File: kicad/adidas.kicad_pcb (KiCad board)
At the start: 2 copper layers, 2 parts

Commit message: v0.1
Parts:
- removed the G*** at (152.4, 96.5)
- added G***: LOGO, DEAD10C5:Adidas, F.Cu at (147.3, 94.0)
- moved G*** 69.7 mm to (221.0, 91.4)

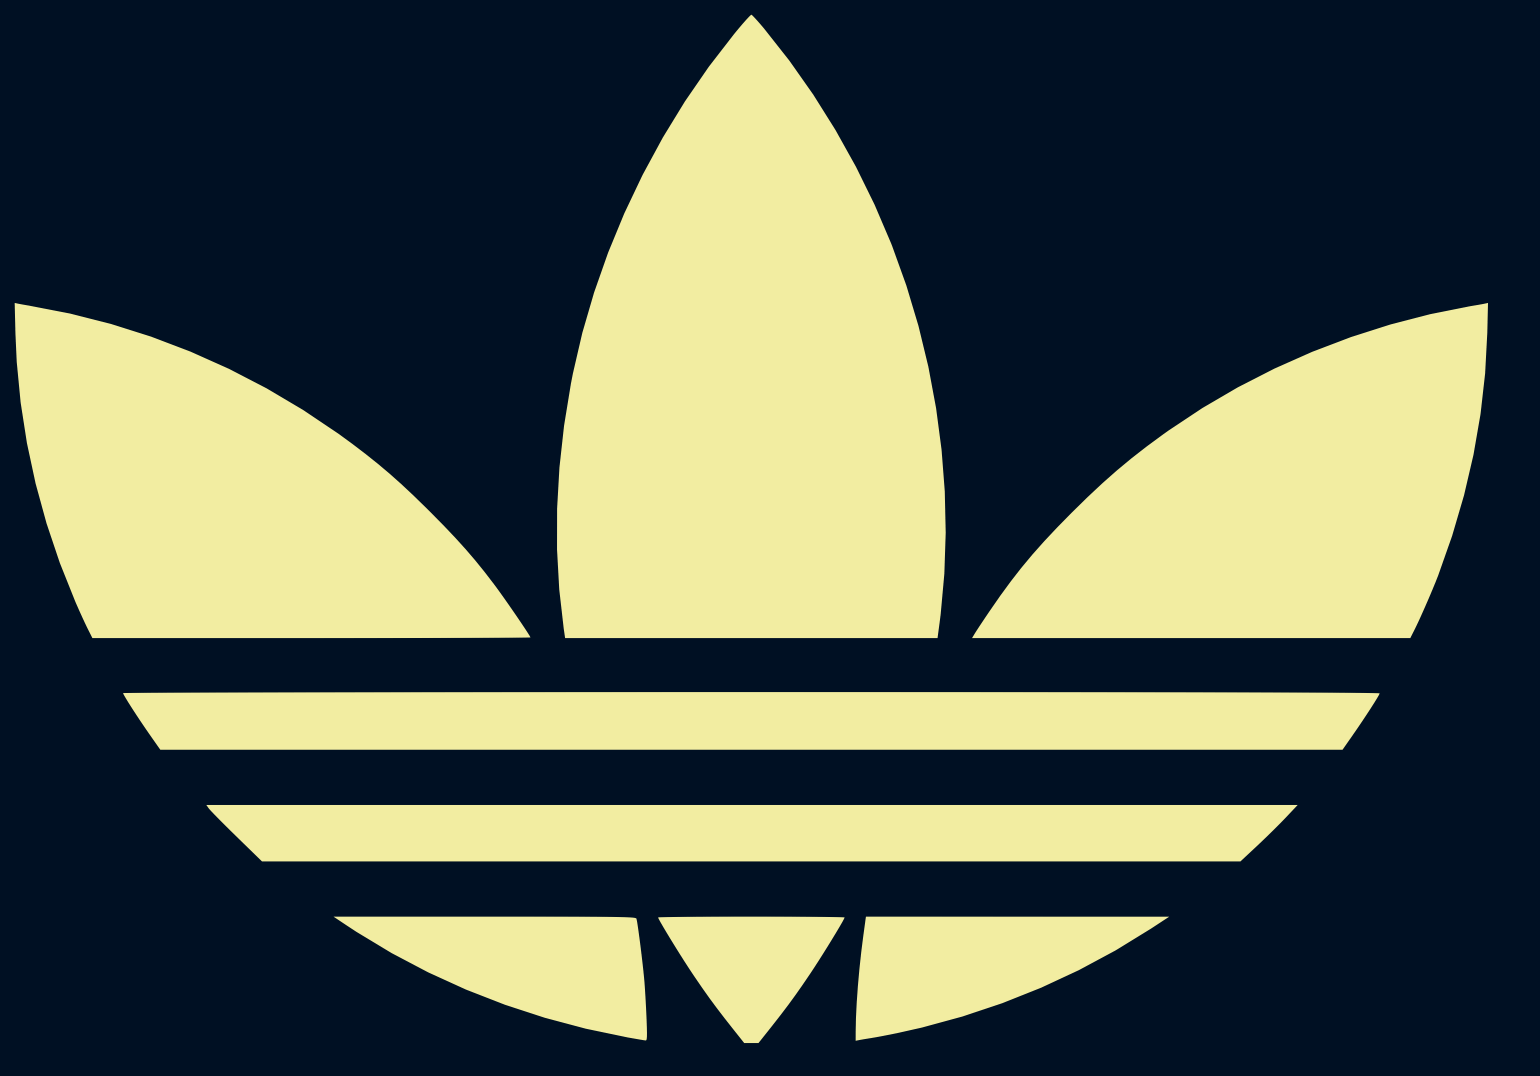
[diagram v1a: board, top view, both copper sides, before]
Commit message: resized art and created outline
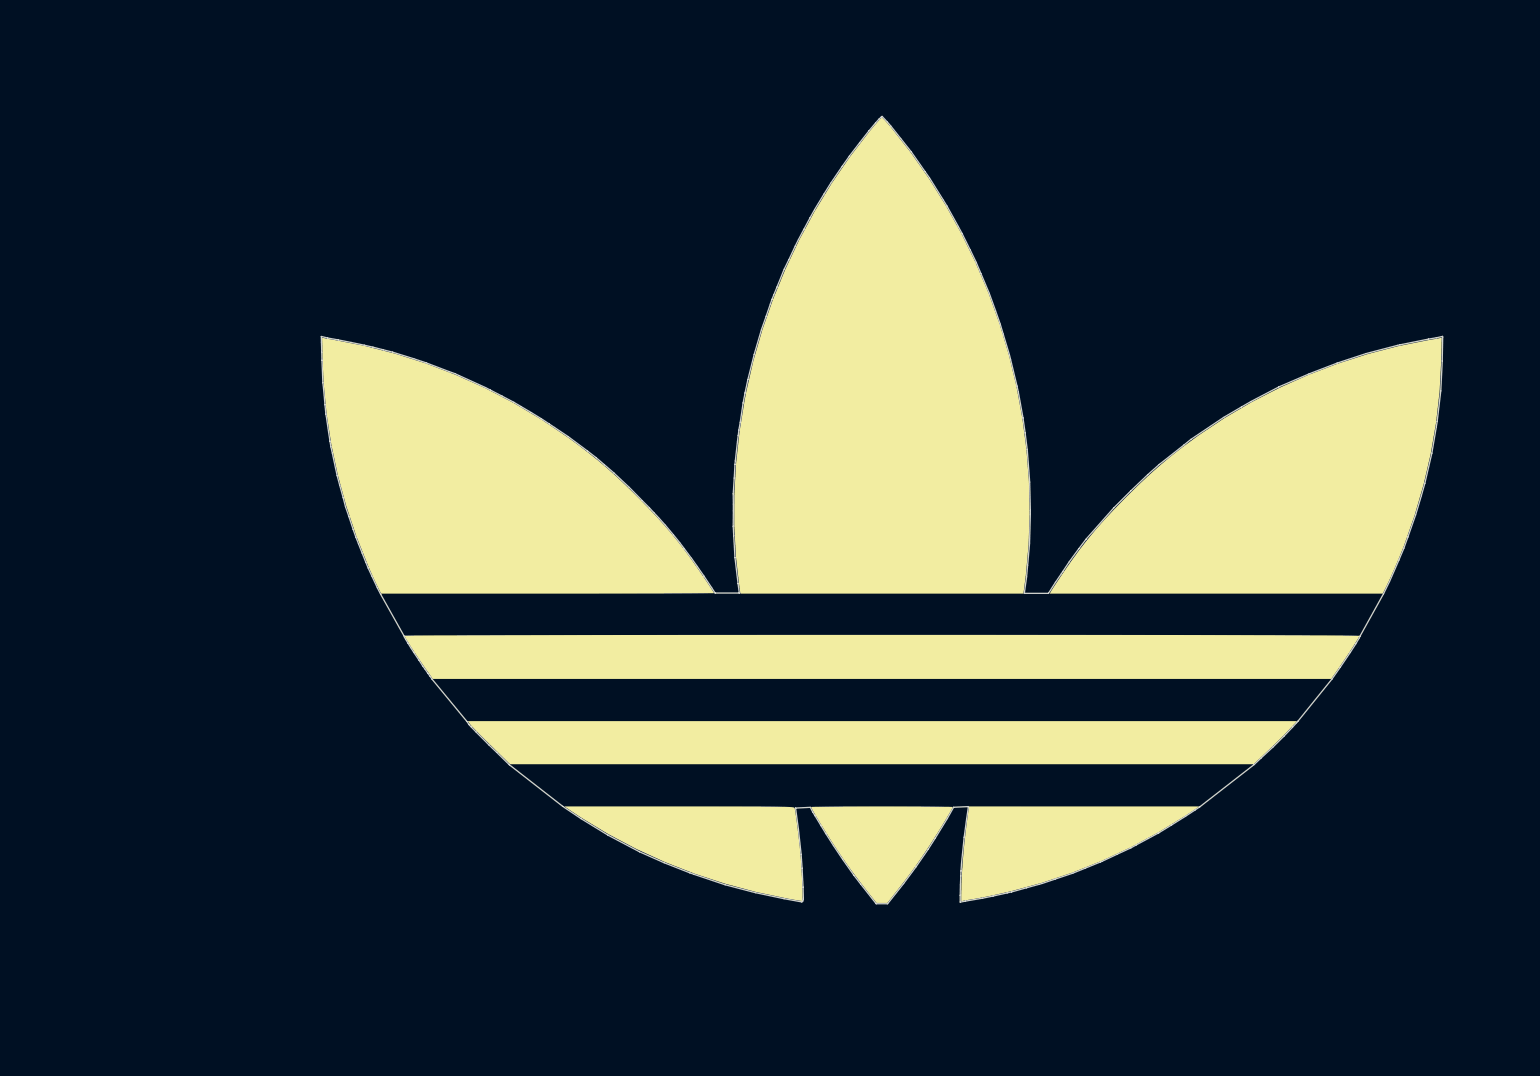
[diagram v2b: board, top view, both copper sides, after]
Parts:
- removed the G*** at (147.3, 94.0)
- added G***: LOGO, Adidas:Adidas_Logo, F.Cu at (165.1, 91.4)
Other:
- board outline added: 152.7 x 107.2 mm

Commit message: updates
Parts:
- added REF**: MountingHole_4.5mm, MountingHole:MountingHole_4.5mm, F.Cu at (165.0, 49.4)
- added REF**: BatteryHolder_Keystone_3002_1x2032, Battery:BatteryHolder_Keystone_3002_1x2032, B.Cu at (164.8, 120.4)
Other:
- board text added: "0.2000 mm / 0.0000 mm"
- board text added: "0.3000 mm"
- board text added: "1.6000 mm"
- board text added: "152.7000 mm x 107.2200 mm"
- board text added: "2"
- board text added: "BOARD CHARACTERISTICS"
- board text added: "Board Thickness:"
- board text added: "Board overall dimensions:"
- board text added: "Castellated pads:"
- board text added: "Copper Finish:"
- board text added: "Copper Layer Count:"
- board text added: "Edge card connectors:"
- board text added: "Impedance Control:"
- board text added: "Min hole diameter:"
- board text added: "Min track/spacing:"
- board text added: "No"
- board text added: "None"
- board text added: "Plated Board Edge:"

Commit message: add mpu6050 part
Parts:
- removed the G*** at (221.0, 91.4)
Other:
- board text added: "мне нравится двигать его двигать его"

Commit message: add 6050 footprint
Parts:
- added REF**: QFN50P400X400X95-24N, Library:QFN50P400X400X95-24N, B.Cu at (165.6, 99.6)
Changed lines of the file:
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@@
     )
+  )
+  (footprint "Library:QFN50P400X400X95-24N" (layer "B.Cu")
+    (at 165.6 99.6 180)
+    (attr through_hole)
+    (fp_text reference "REF**" (at 1.17756 3.64297) (layer "B.SilkS") hide
+      (effects (font (size 1.002189 1.002189) (thickness 0.15)) (justify mirror))
+    )
+    (fp_text value "QFN50P400X400X95-24N" (at 10.71558 -3.369915) (layer "B.Fab") hide
+      (effects (font (size 1.001457 1.001457) (thickness 0.15)) (justify mirror))
+    )
+    (fp_line (start 2.05 -1.56) (end 2.05 -2.05) (layer "B.SilkS") (width 0.127))
+    (fp_line (start -2.05 -2.05) (end -2.05 -1.56) (layer "B.SilkS") (width 0.127))
+    (fp_line (start 2.05 -2.05) (end 1.56 -2.05) (layer "B.SilkS") (width 0.127))
+    (fp_line (start -1.56 -2.05) (end -2.05 -2.05) (layer "B.SilkS") (width 0.127))
+    (fp_line (start 2.05 2.05) (end 2.05 1.56) (layer "B.SilkS") (width 0.127))
+    (fp_line (start -1.56 2.05) (end -2.05 2.05) (layer "B.SilkS") (width 0.127))
+    (fp_line (start 1.56 2.05) (end 2.05 2.05) (layer "B.SilkS") (width 0.127))
+    (fp_line (start -2.05 1.56) (end -2.05 2.05) (layer "B.SilkS") (width 0.127))
+    (fp_circle (center -3 1.3) (end -2.9 1.3) (layer "B.SilkS") (width 0.2) (fill none))
+    (fp_line (start -2.62 -2.62) (end -2.62 2.62) (layer "B.CrtYd") (width 0.05))
+    (fp_line (start 2.62 2.62) (end 2.62 -2.62) (layer "B.CrtYd") (width 0.05))
+    (fp_line (start -2.62 2.62) (end 2.62 2.62) (layer "B.CrtYd") (width 0.05))
+    (fp_line (start 2.62 -2.62) (end -2.62 -2.62) (layer "B.CrtYd") (width 0.05))
+    (fp_line (start -2.05 2.05) (end -2.05 -2.05) (layer "B.Fab") (width 0.127))
+    (fp_line (start 2.05 2.05) (end 2.05 -2.05) (layer "B.Fab") (width 0.127))
+    (fp_line (start 2.05 2.05) (end -2.05 2.05) (layer "B.Fab") (width 0.127))
+    (fp_line (start 2.05 -2.05) (end -2.05 -2.05) (layer "B.Fab") (width 0.127))
+    (pad "1" smd rect (at -1.97 1.25 180) (size 0.79 0.26) (layers "B.Cu" "B.Paste" "B.Mask"))
+    (pad "2" smd rect (at -1.97 0.75 180) (size 0.79 0.26) (layers "B.Cu" "B.Paste" "B.Mask"))
+    (pad "3" smd rect (at -1.97 0.25 180) (size 0.79 0.26) (layers "B.Cu" "B.Paste" "B.Mask"))
+    (pad "4" smd rect (at -1.97 -0.25 180) (size 0.79 0.26) (layers "B.Cu" "B.Paste" "B.Mask"))
+    (pad "5" smd rect (at -1.97 -0.75 180) (size 0.79 0.26) (layers "B.Cu" "B.Paste" "B.Mask"))
+    (pad "6" smd rect (at -1.97 -1.25 180) (size 0.79 0.26) (layers "B.Cu" "B.Paste" "B.Mask"))
+    (pad "7" smd rect (at -1.25 -1.97 90) (size 0.79 0.26) (layers "B.Cu" "B.Paste" "B.Mask"))
+    (pad "8" smd rect (at -0.75 -1.97 90) (size 0.79 0.26) (layers "B.Cu" "B.Paste" "B.Mask"))
+    (pad "9" smd rect (at -0.25 -1.97 90) (size 0.79 0.26) (layers "B.Cu" "B.Paste" "B.Mask"))
+    (pad "10" smd rect (at 0.25 -1.97 90) (size 0.79 0.26) (layers "B.Cu" "B.Paste" "B.Mask"))
+    (pad "11" smd rect (at 0.75 -1.97 90) (size 0.79 0.26) (layers "B.Cu" "B.Paste" "B.Mask"))
+    (pad "12" smd rect (at 1.25 -1.97 90) (size 0.79 0.26) (layers "B.Cu" "B.Paste" "B.Mask"))
+    (pad "13" smd rect (at 1.97 -1.25) (size 0.79 0.26) (layers "B.Cu" "B.Paste" "B.Mask"))
+    (pad "14" smd rect (at 1.97 -0.75) (size 0.79 0.26) (layers "B.Cu" "B.Paste" "B.Mask"))
+    (pad "15" smd rect (at 1.97 -0.25) (size 0.79 0.26) (layers "B.Cu" "B.Paste" "B.Mask"))
+    (pad "16" smd rect (at 1.97 0.25) (size 0.79 0.26) (layers "B.Cu" "B.Paste" "B.Mask"))
+    (pad "17" smd rect (at 1.97 0.75) (size 0.79 0.26) (layers "B.Cu" "B.Paste" "B.Mask"))
+    (pad "18" smd rect (at 1.97 1.25) (size 0.79 0.26) (layers "B.Cu" "B.Paste" "B.Mask"))
+    (pad "19" smd rect (at 1.25 1.97 270) (size 0.79 0.26) (layers "B.Cu" "B.Paste" "B.Mask"))
+    (pad "20" smd rect (at 0.75 1.97 270) (size 0.79 0.26) (layers "B.Cu" "B.Paste" "B.Mask"))
+    (pad "21" smd rect (at 0.25 1.97 270) (size 0.79 0.26) (layers "B.Cu" "B.Paste" "B.Mask"))
+    (pad "22" smd rect (at -0.25 1.97 270) (size 0.79 0.26) (layers "B.Cu" "B.Paste" "B.Mask"))
+    (pad "23" smd rect (at -0.75 1.97 270) (size 0.79 0.26) (layers "B.Cu" "B.Paste" "B.Mask"))
+    (pad "24" smd rect (at -1.25 1.97 270) (size 0.79 0.26) (layers "B.Cu" "B.Paste" "B.Mask"))
   )
   (gr_line (start 159.75 138.97) (end 161.3 141.17) (layer "Edge.Cuts") (width 0.1))

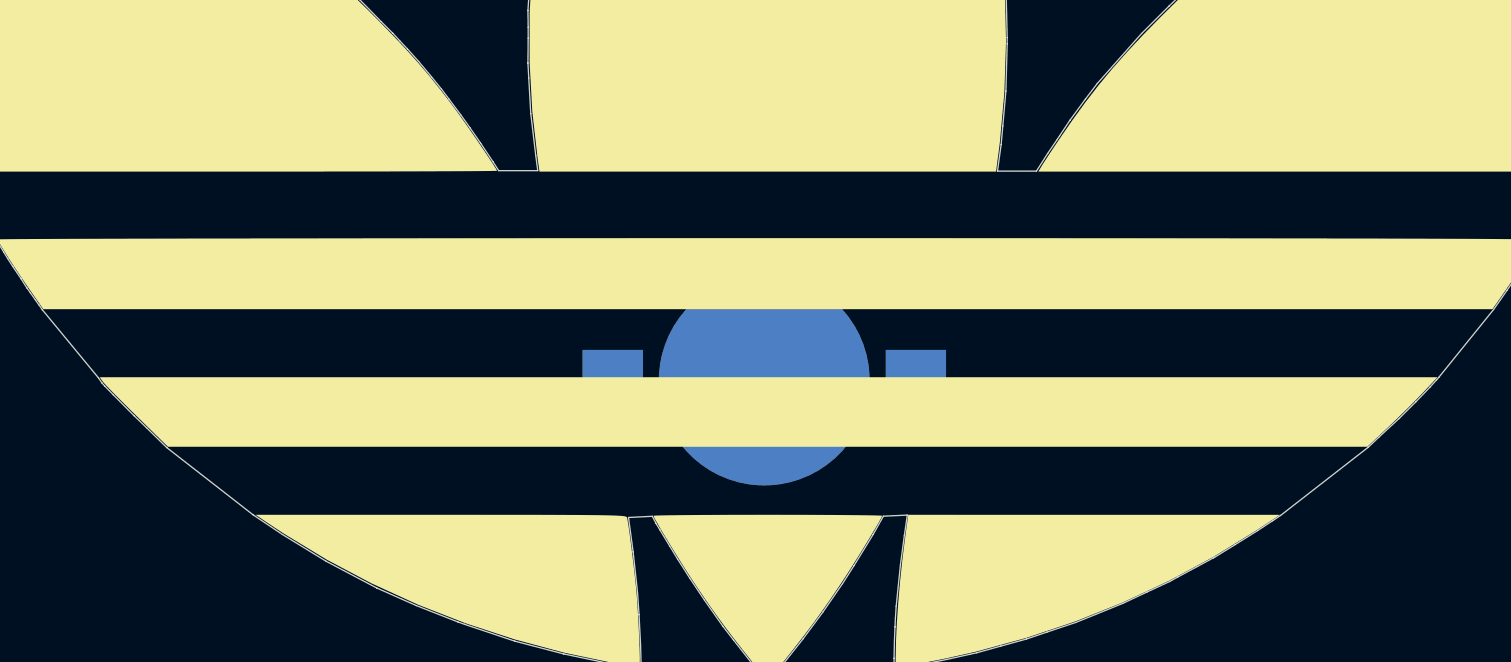
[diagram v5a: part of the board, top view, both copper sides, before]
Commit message: add a microcontroller (#6)
* add a microcontroller

* test ISP header

* test LED placement

* test LED placement
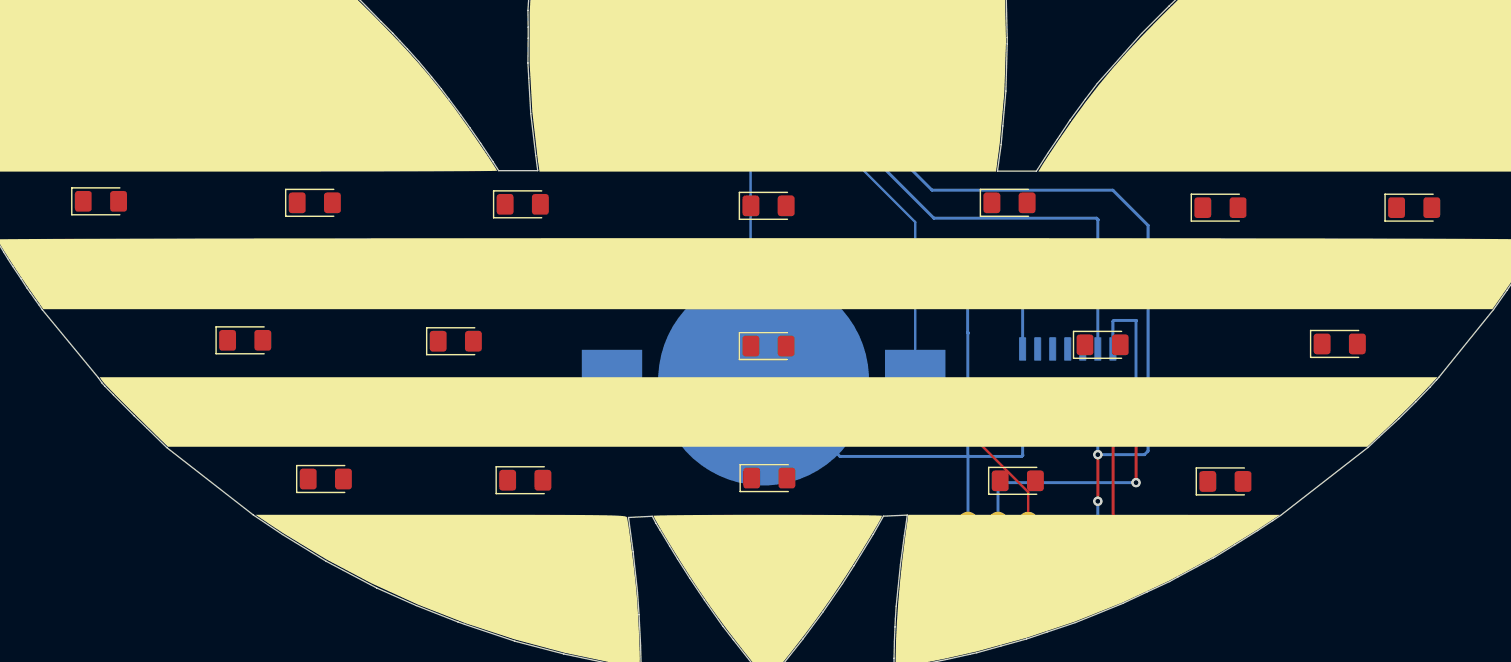
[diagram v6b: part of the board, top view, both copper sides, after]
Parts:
- added REF**: D_1206_3216Metric_Pad1.42x1.75mm_HandSolder, Diode_SMD:D_1206_3216Metric_Pad1.42x1.75mm_HandSolder, F.Cu at (213.4, 117.3)
- added REF**: D_1206_3216Metric_Pad1.42x1.75mm_HandSolder, Diode_SMD:D_1206_3216Metric_Pad1.42x1.75mm_HandSolder, F.Cu at (144.6, 128.9)
- added REF**: D_1206_3216Metric_Pad1.42x1.75mm_HandSolder, Diode_SMD:D_1206_3216Metric_Pad1.42x1.75mm_HandSolder, F.Cu at (219.7, 105.8)
- added REF**: D_1206_3216Metric_Pad1.42x1.75mm_HandSolder, Diode_SMD:D_1206_3216Metric_Pad1.42x1.75mm_HandSolder, F.Cu at (165.2, 117.5)
- added REF**: D_1206_3216Metric_Pad1.42x1.75mm_HandSolder, Diode_SMD:D_1206_3216Metric_Pad1.42x1.75mm_HandSolder, F.Cu at (193.4, 117.4)
- added REF**: D_1206_3216Metric_Pad1.42x1.75mm_HandSolder, Diode_SMD:D_1206_3216Metric_Pad1.42x1.75mm_HandSolder, F.Cu at (138.8, 117.1)
- added REF**: D_1206_3216Metric_Pad1.42x1.75mm_HandSolder, Diode_SMD:D_1206_3216Metric_Pad1.42x1.75mm_HandSolder, F.Cu at (121.0, 117.0)
- added REF**: D_1206_3216Metric_Pad1.42x1.75mm_HandSolder, Diode_SMD:D_1206_3216Metric_Pad1.42x1.75mm_HandSolder, F.Cu at (203.3, 105.8)
- added REF**: D_1206_3216Metric_Pad1.42x1.75mm_HandSolder, Diode_SMD:D_1206_3216Metric_Pad1.42x1.75mm_HandSolder, F.Cu at (144.4, 105.6)
- added REF**: D_1206_3216Metric_Pad1.42x1.75mm_HandSolder, Diode_SMD:D_1206_3216Metric_Pad1.42x1.75mm_HandSolder, F.Cu at (165.2, 105.7)
- added REF**: PinHeader_2x03_P2.54mm_Vertical, Connector_PinHeader_2.54mm:PinHeader_2x03_P2.54mm_Vertical, B.Cu at (187.1, 134.9)
- added REF**: D_1206_3216Metric_Pad1.42x1.75mm_HandSolder, Diode_SMD:D_1206_3216Metric_Pad1.42x1.75mm_HandSolder, F.Cu at (203.7, 129.0)
- added REF**: SOIC127P599X175-14N, at841:SOIC127P599X175-14N, B.Cu at (190.4, 120.2)
- added REF**: TestPoint_2Pads_Pitch2.54mm_Drill0.8mm, TestPoint:TestPoint_2Pads_Pitch2.54mm_Drill0.8mm, B.Cu at (182.0, 113.3)
- added REF**: D_1206_3216Metric_Pad1.42x1.75mm_HandSolder, Diode_SMD:D_1206_3216Metric_Pad1.42x1.75mm_HandSolder, F.Cu at (126.9, 105.4)
- added REF**: D_1206_3216Metric_Pad1.42x1.75mm_HandSolder, Diode_SMD:D_1206_3216Metric_Pad1.42x1.75mm_HandSolder, F.Cu at (108.8, 105.3)
- added REF**: D_1206_3216Metric_Pad1.42x1.75mm_HandSolder, Diode_SMD:D_1206_3216Metric_Pad1.42x1.75mm_HandSolder, F.Cu at (186.2, 128.9)
- added REF**: D_1206_3216Metric_Pad1.42x1.75mm_HandSolder, Diode_SMD:D_1206_3216Metric_Pad1.42x1.75mm_HandSolder, F.Cu at (165.2, 128.7)
- added REF**: D_1206_3216Metric_Pad1.42x1.75mm_HandSolder, Diode_SMD:D_1206_3216Metric_Pad1.42x1.75mm_HandSolder, F.Cu at (185.5, 105.4)
- added REF**: D_1206_3216Metric_Pad1.42x1.75mm_HandSolder, Diode_SMD:D_1206_3216Metric_Pad1.42x1.75mm_HandSolder, F.Cu at (127.8, 128.8)
- moved REF** 0.73 mm to (164.9, 99.4), turned to -90 degrees
- moved REF** 0.06 mm to (164.7, 120.4)
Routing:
- net (no net): track 0.00 -> 340.2 mm, vias 0 -> 6
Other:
- board text added: "+"
- board text added: "-"
- board text added: "MISO"
- board text added: "MOSI"
- board text added: "SCK"
- board text added: "Мощность"
- board text added: "приседать готов"
- board text removed: "мне нравится двигать его двигать его"
